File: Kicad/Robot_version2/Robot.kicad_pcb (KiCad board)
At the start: 2 copper layers, 149 x 78.5 mm, 52 parts, among them J1 PositiveBus, J10 LORA, J11 RELAY HEADER, J12 X8R HEADER, J13 SENSOR 1, J14 SENSOR 2, J15 SENSOR 3, J16 SENSOR 4, J2 NegativeBus, J3 PIN HEADER DE0-NANO POWER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

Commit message: updated schematic and layout for shield v2
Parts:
- added J17: BreakoutHeader, Robot:PinHeader_1x06_P2.54mm_Vertical, F.Cu at (59.6, 40.6)
- added MH7: MountingHole, Robot:MountingHole_4.3mm_M4, F.Cu at (76.4, 24.6)
- moved MH6 12.2 mm to (60.2, 25.4)
- moved J3 2.24 mm to (3.67, 37.9)
- moved J10 0.83 mm to (27.1, 56.2)
- moved JP2 0.60 mm to (64.4, 44.9)
- moved J9 0.60 mm to (41.5, 40.6)
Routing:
- net Net-(J6-Pad2): track 25.1 -> 13.4 mm
- net Net-(J17-Pad6): track 0.27 -> 4.64 mm
- net Net-(J17-Pad2): track 0.00 -> 4.37 mm
- net Net-(J17-Pad1): track 0.00 -> 4.37 mm
- net Net-(J17-Pad4): track 0.00 -> 4.37 mm
- net Net-(J17-Pad3): track 0.07 -> 4.44 mm
- net Net-(J17-Pad5): track 0.00 -> 4.03 mm
- net Net-(C3-Pad1): track 16.6 -> 19.0 mm
- net Net-(J6-Pad1): track 19.3 -> 17.3 mm
- net GND: track 523.6 -> 525.2 mm
- net TX: track 9.20 -> 8.42 mm
- net RI5: track 61.4 -> 62.0 mm
- net RI3: track 59.0 -> 59.6 mm
- net SENSOR4: track 33.8 -> 34.4 mm

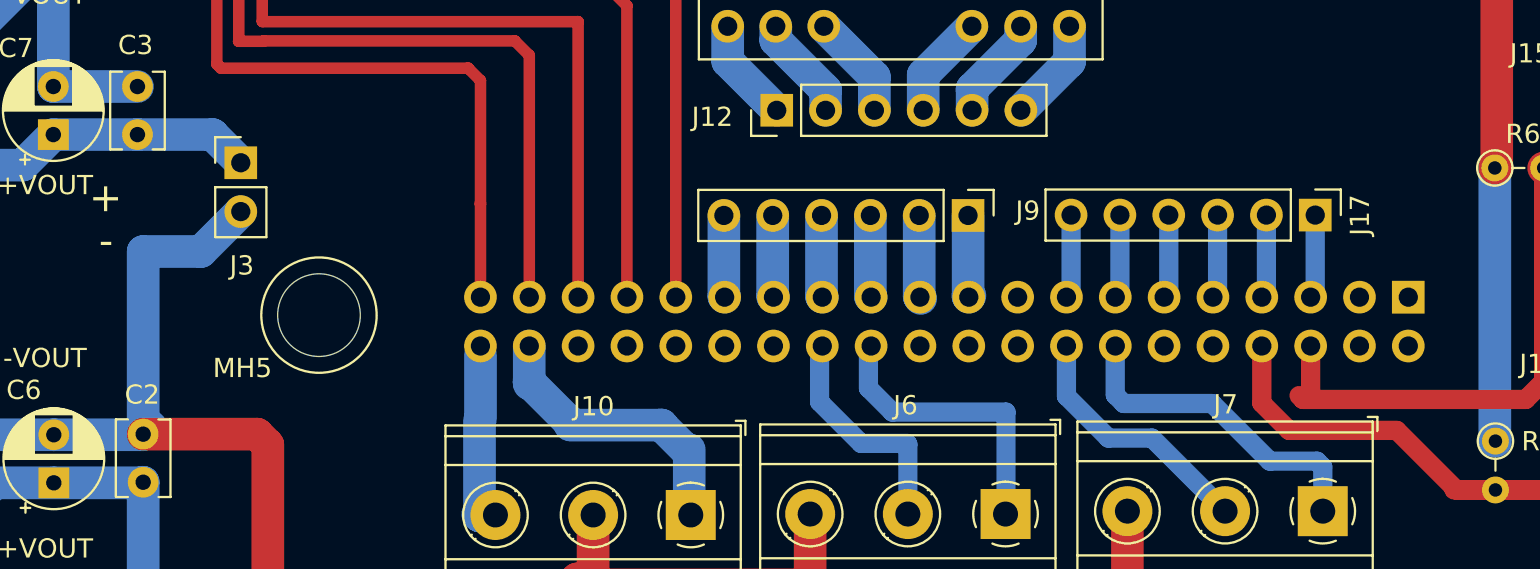
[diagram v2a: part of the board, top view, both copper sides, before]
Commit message: moved jp2 and j3 -0.3X and -0.15Y
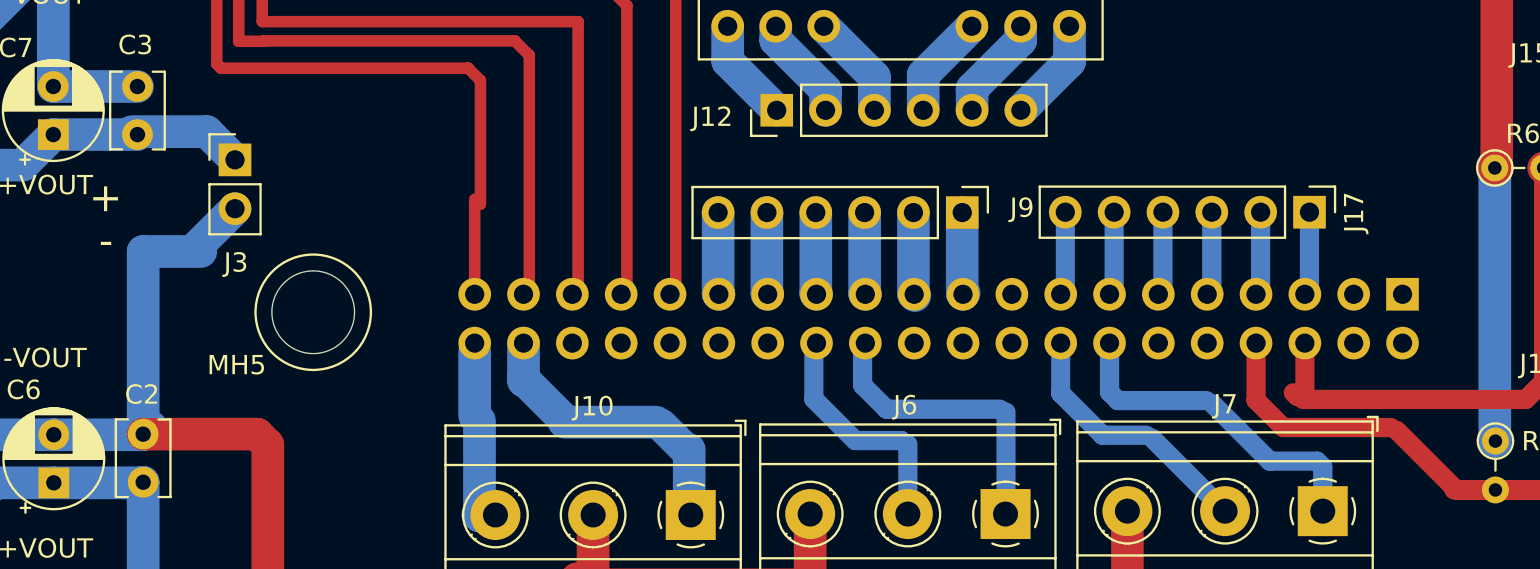
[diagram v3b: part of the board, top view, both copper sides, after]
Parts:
- moved JP2 0.34 mm to (64.1, 44.7)
- moved J17 0.34 mm to (59.3, 40.5)
- moved MH5 0.34 mm to (7.44, 45.7)
- moved J3 0.34 mm to (3.37, 37.7)
- moved J9 0.34 mm to (41.2, 40.5)
